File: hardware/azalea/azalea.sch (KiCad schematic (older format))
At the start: 88 parts, among them J1 NEIGHBOR1, J2 NEIGHBOR2, J3 USB-MICRO-B-SHIELDED, J4 USB-MICRO-B-SHIELDED, J5 JTAG, J7 BONUS_ROW, SW1 DFU, SW2 RESET, U1 LPC4330FBD144, U2 W25Q16DV, U3 AP7333, U4 IP4220CZ6, U5 NX5P2553GV, X1 XTAL4PIN, X2 RTC_XTAL

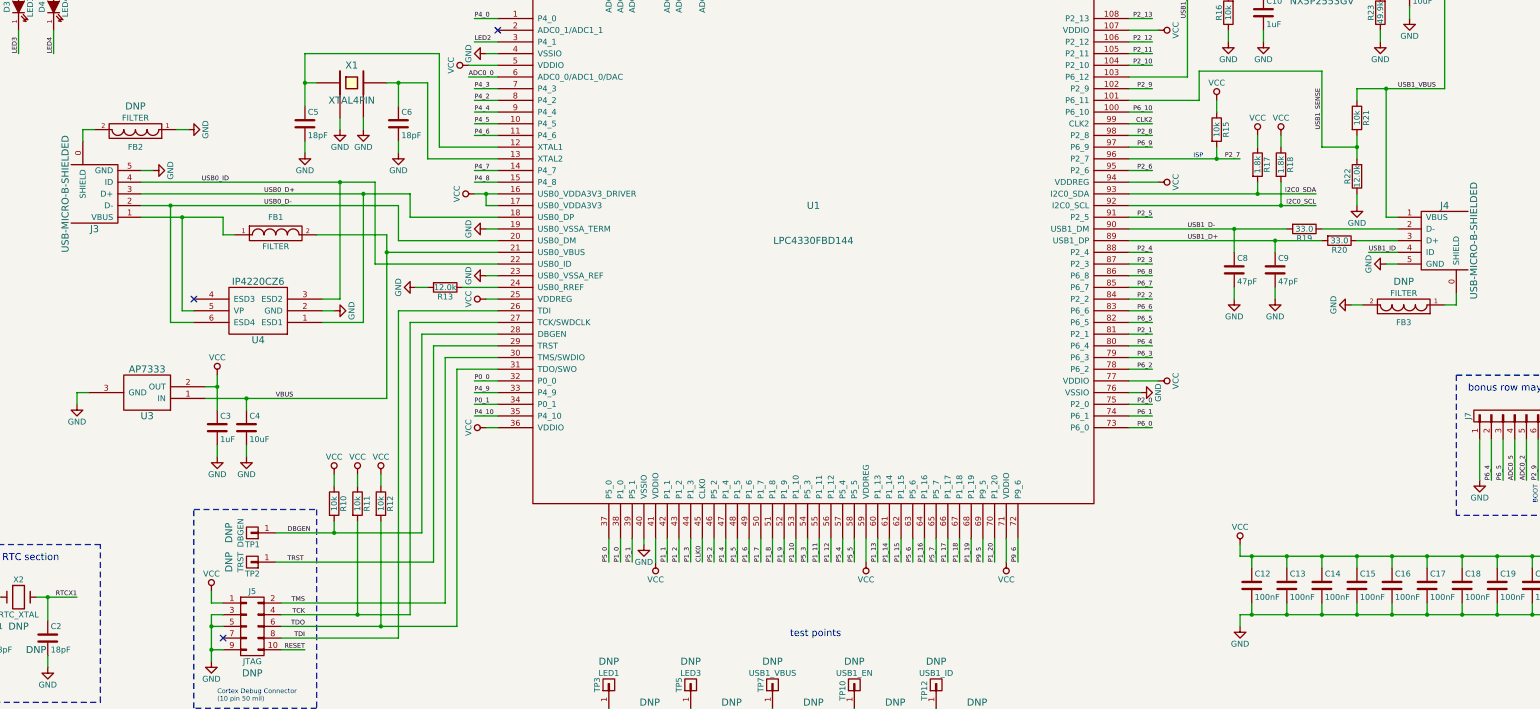
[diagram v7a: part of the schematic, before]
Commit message: azalea: corrected DRC errors
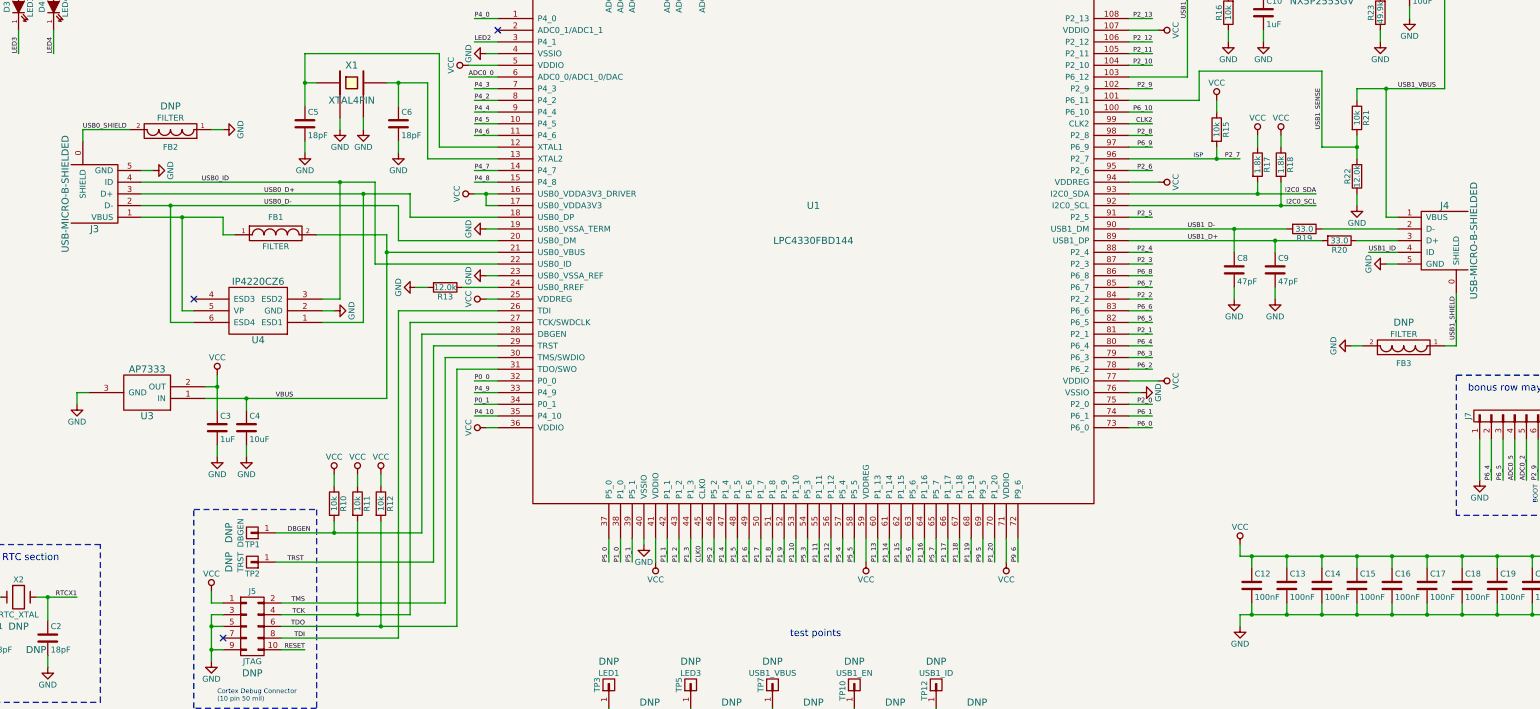
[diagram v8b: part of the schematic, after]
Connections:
- net USB0_SHIELD: now reaches FB2.2, J3.0 (SHIELD)
- net USB1_SHIELD: now reaches FB3.1, J4.0 (SHIELD)
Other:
- moved on the sheet: FB2, FB3
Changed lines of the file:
@@
 L FILTER FB2
 U 1 1 560950C5
-P 2750 4550
-F 0 "FB2" H 2750 4700 50  0000 C CNN
-F 1 "FILTER" H 2750 4450 50  0000 C CNN
-F 2 "gsg-modules:0603" H 2750 4550 60  0001 C CNN
-F 3 "" H 2750 4550 60  0000 C CNN
-F 4 "Murata" H 2750 4550 60  0001 C CNN "Manufacturer"
-F 5 "BLM21PG221SN1D" H 2750 4550 60  0001 C CNN "Part Number"
-F 6 "FERRITE CHIP 220 OHM 2000MA 0805" H 2750 4550 60  0001 C CNN "Description"
-F 7 "DNP" H 2750 4350 60  0000 C CNN "Note"
-	1    2750 4550
+P 3050 4550
+F 0 "FB2" H 3050 4700 50  0000 C CNN
+F 1 "FILTER" H 3050 4450 50  0000 C CNN
+F 2 "gsg-modules:0603" H 3050 4550 60  0001 C CNN
+F 3 "" H 3050 4550 60  0000 C CNN
+F 4 "Murata" H 3050 4550 60  0001 C CNN "Manufacturer"
+F 5 "BLM21PG221SN1D" H 3050 4550 60  0001 C CNN "Part Number"
+F 6 "FERRITE CHIP 220 OHM 2000MA 0805" H 3050 4550 60  0001 C CNN "Description"
+F 7 "DNP" H 3050 4350 60  0000 C CNN "Note"
+	1    3050 4550
 	-1   0    0    1
 $EndComp
@@
 L GND #PWR073
 U 1 1 5609538F
-P 3200 4550
-F 0 "#PWR073" H 3200 4300 50  0001 C CNN
-F 1 "GND" H 3200 4400 50  0000 C CNN
-F 2 "" H 3200 4550 60  0000 C CNN
-F 3 "" H 3200 4550 60  0000 C CNN
-	1    3200 4550
+P 3500 4550
+F 0 "#PWR073" H 3500 4300 50  0001 C CNN
+F 1 "GND" H 3500 4400 50  0000 C CNN
+F 2 "" H 3500 4550 60  0000 C CNN
+F 3 "" H 3500 4550 60  0000 C CNN
+	1    3500 4550
 	0    -1   -1   0
 $EndComp
@@
 L FILTER FB3
 U 1 1 56095F33
-P 13600 6050
-F 0 "FB3" H 13600 6200 50  0000 C CNN
-F 1 "FILTER" H 13600 5950 50  0000 C CNN
-F 2 "gsg-modules:0603" H 13600 6050 60  0001 C CNN
-F 3 "" H 13600 6050 60  0000 C CNN
-F 4 "Murata" H 13600 6050 60  0001 C CNN "Manufacturer"
-F 5 "BLM21PG221SN1D" H 13600 6050 60  0001 C CNN "Part Number"
-F 6 "FERRITE CHIP 220 OHM 2000MA 0805" H 13600 6050 60  0001 C CNN "Description"
-F 7 "DNP" H 13600 5850 60  0000 C CNN "Note"
-	1    13600 6050
+P 13600 6400
+F 0 "FB3" H 13600 6550 50  0000 C CNN
+F 1 "FILTER" H 13600 6300 50  0000 C CNN
+F 2 "gsg-modules:0603" H 13600 6400 60  0001 C CNN
+F 3 "" H 13600 6400 60  0000 C CNN
+F 4 "Murata" H 13600 6400 60  0001 C CNN "Manufacturer"
+F 5 "BLM21PG221SN1D" H 13600 6400 60  0001 C CNN "Part Number"
+F 6 "FERRITE CHIP 220 OHM 2000MA 0805" H 13600 6400 60  0001 C CNN "Description"
+F 7 "DNP" H 13600 6200 60  0000 C CNN "Note"
+	1    13600 6400
 	-1   0    0    1
 $EndComp
@@
 L GND #PWR074
 U 1 1 56095F39
-P 13150 6050
-F 0 "#PWR074" H 13150 5800 50  0001 C CNN
-F 1 "GND" H 13150 5900 50  0000 C CNN
-F 2 "" H 13150 6050 60  0000 C CNN
-F 3 "" H 13150 6050 60  0000 C CNN
-	1    13150 6050
+P 13150 6400
+F 0 "#PWR074" H 13150 6150 50  0001 C CNN
+F 1 "GND" H 13150 6250 50  0000 C CNN
+F 2 "" H 13150 6400 60  0000 C CNN
+F 3 "" H 13150 6400 60  0000 C CNN
+	1    13150 6400
 	0    1    1    0
 $EndComp
@@
 	5850 5500 5000 5500
 Wire Wire Line
-	5000 5500 5000 5200
+	5000 5200 5000 5500
 Wire Wire Line
 	5750 5800 5850 5800
@@
 	4300 5450 4900 5450
 Wire Wire Line
-	4900 5450 4900 6850
+	4900 6850 4900 5450
 Wire Wire Line
 	3700 6850 3700 6950
@@
 	5850 5700 4800 5700
 Wire Wire Line
-	4800 5700 4800 5000
-Wire Wire Line
-	4800 5000 2800 5000
+	4800 5000 4800 5700
+Wire Wire Line
+	2800 5000 4800 5000
 Wire Wire Line
 	2800 4900 2900 4900
@@
 	5850 4800 5250 4800
 Wire Wire Line
-	5250 4800 5250 4150
-Wire Wire Line
-	5250 4150 4900 4150
+	5250 4150 5250 4800
+Wire Wire Line
+	4900 4150 5250 4150
 Wire Wire Line
 	5850 4700 5350 4700
@@
 Connection ~ 3450 6750
 Wire Wire Line
-	4900 6850 3350 6850
+	3350 6850 4900 6850
 Connection ~ 3700 6850
 Wire Wire Line
@@
 	5850 6600 5500 6600
 Wire Wire Line
-	5500 6600 5500 8800
-Wire Wire Line
-	5500 8800 4000 8800
+	5500 8800 5500 6600
+Wire Wire Line
+	4000 8800 5500 8800
 Wire Wire Line
 	4200 9000 4000 9000
 Wire Wire Line
-	5200 6300 5200 8000
-Wire Wire Line
-	5200 8000 3950 8000
+	5200 8000 5200 6300
+Wire Wire Line
+	3950 8000 5200 8000
 Wire Wire Line
 	4450 8000 4450 7900
@@
 	9950 10250 9950 9850
 Wire Wire Line
-	3200 4550 3100 4550
-Wire Wire Line
-	2400 4550 2300 4550
+	3500 4550 3400 4550
+Wire Wire Line
+	2700 4550 2300 4550
 Wire Wire Line
 	2300 4550 2300 4650
 Wire Wire Line
-	13150 6050 13250 6050
-Wire Wire Line
-	13950 6050 14050 6050
-Wire Wire Line
-	14050 6050 14050 5950
+	13150 6400 13250 6400
+Wire Wire Line
+	13950 6400 14050 6400
+Wire Wire Line
+	14050 6400 14050 5950
 Wire Wire Line
 	5650 6700 5850 6700
@@
 USB1_D+
 Wire Wire Line
-	5000 5200 2800 5200
+	2800 5200 5000 5200
 Connection ~ 3050 5200
 Wire Wire Line
@@
 	3050 6200 3050 5200
 NoConn ~ 3250 6000
+Text Label 2300 4550 0    40   ~ 0
+USB0_SHIELD
+Text Label 14050 6350 1    40   ~ 0
+USB1_SHIELD
 $EndSCHEMATC
